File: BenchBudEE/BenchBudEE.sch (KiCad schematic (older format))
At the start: 0 parts

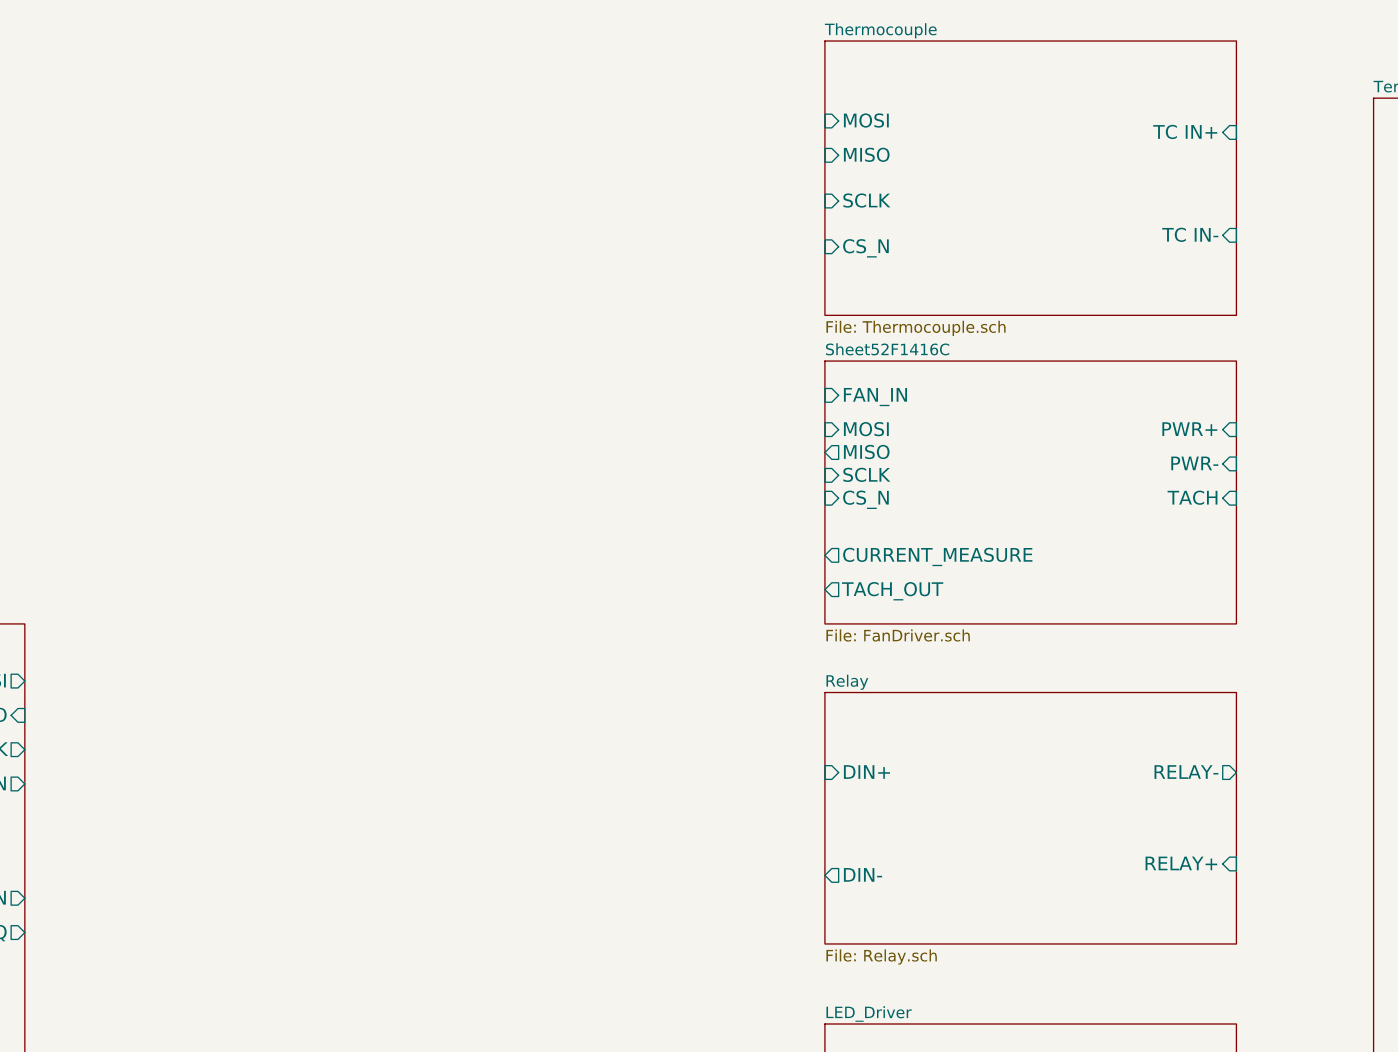
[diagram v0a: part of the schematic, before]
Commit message: Power module blocked out + added power adjustment monitor module
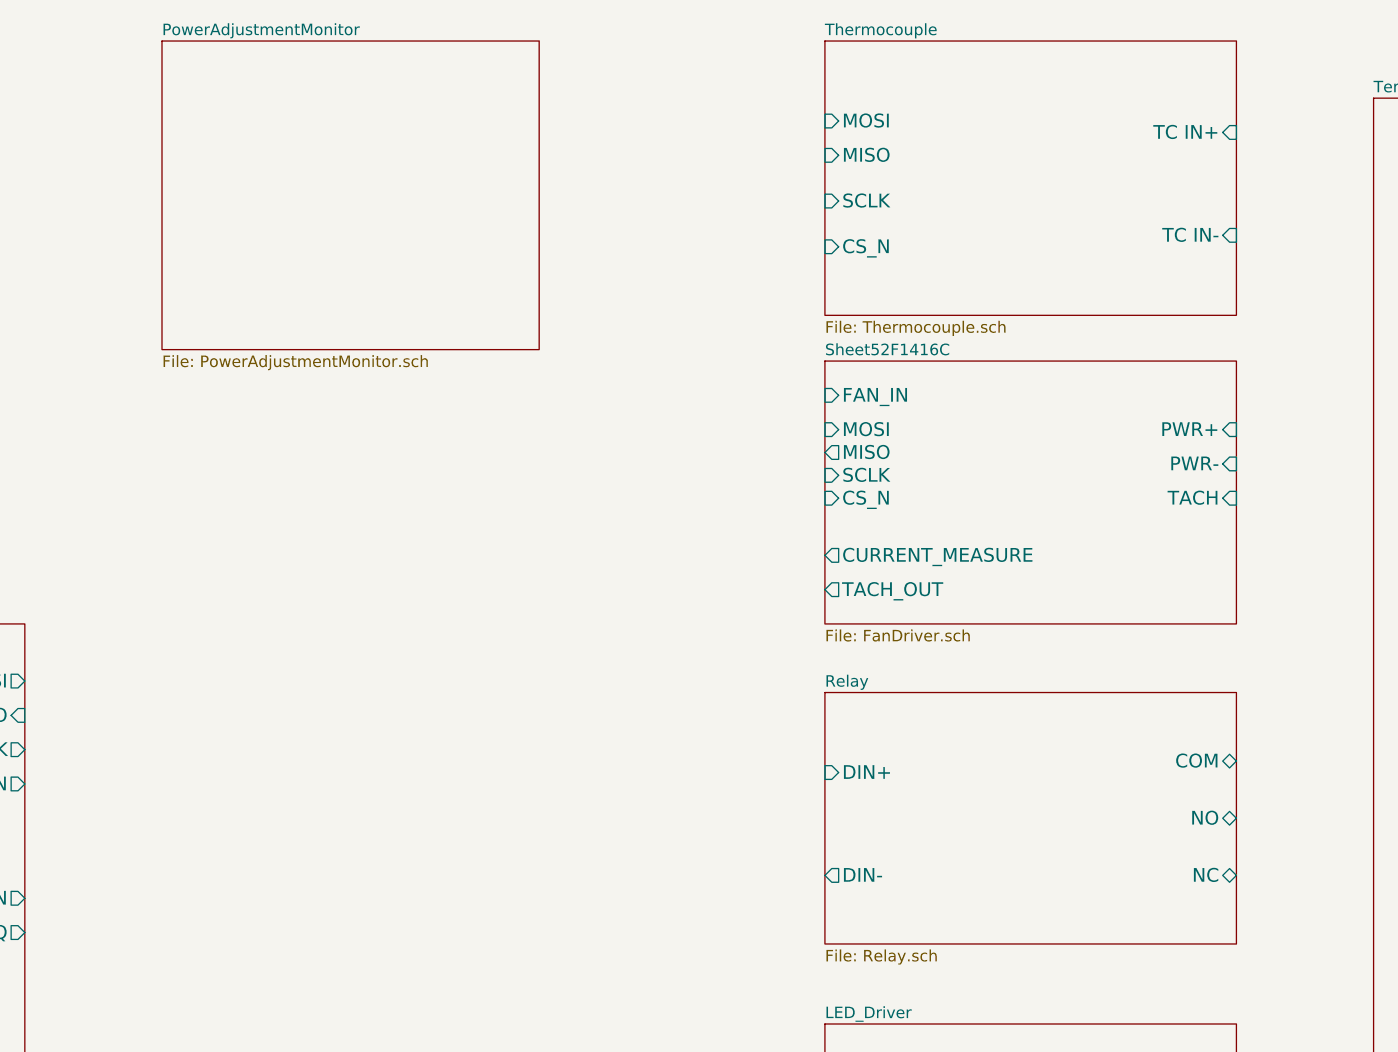
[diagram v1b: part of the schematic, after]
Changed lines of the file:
@@
 $Descr A4 11693 8268
 encoding utf-8
-Sheet 1 8
+Sheet 1 9
 Title ""
 Date "5 feb 2014"
@@
 F2 "DIN+" I L 7400 4250 60
 F3 "DIN-" O L 7400 4700 60
-F4 "RELAY-" O R 9200 4250 60
-F5 "RELAY+" I R 9200 4650 60
+F4 "NO" B R 9200 4450 60
+F5 "NC" B R 9200 4700 60
+F6 "COM" B R 9200 4200 60
 $EndSheet
 $Sheet
@@
 F7 "CS_N" I L 7400 1950 60
 $EndSheet
+$Sheet
+S 4500 1050 1650 1350
+U 52F2C572
+F0 "PowerAdjustmentMonitor" 50
+F1 "PowerAdjustmentMonitor.sch" 50
+$EndSheet
 $EndSCHEMATC

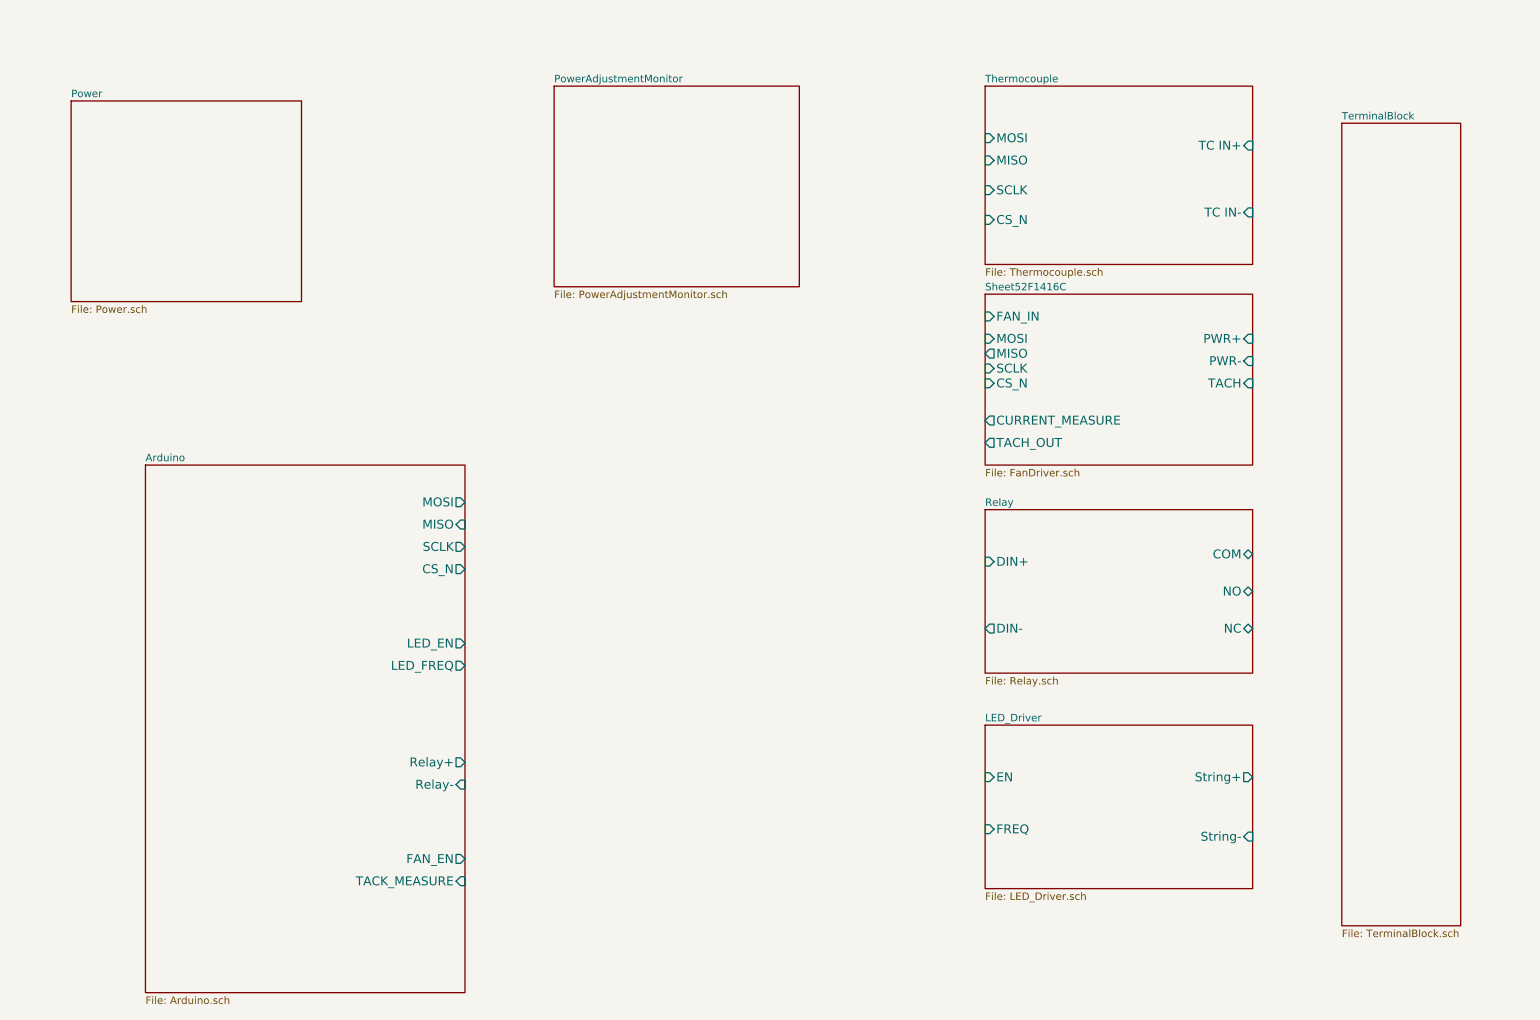
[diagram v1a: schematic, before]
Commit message: Power monitor module blocked out (needs tidying)
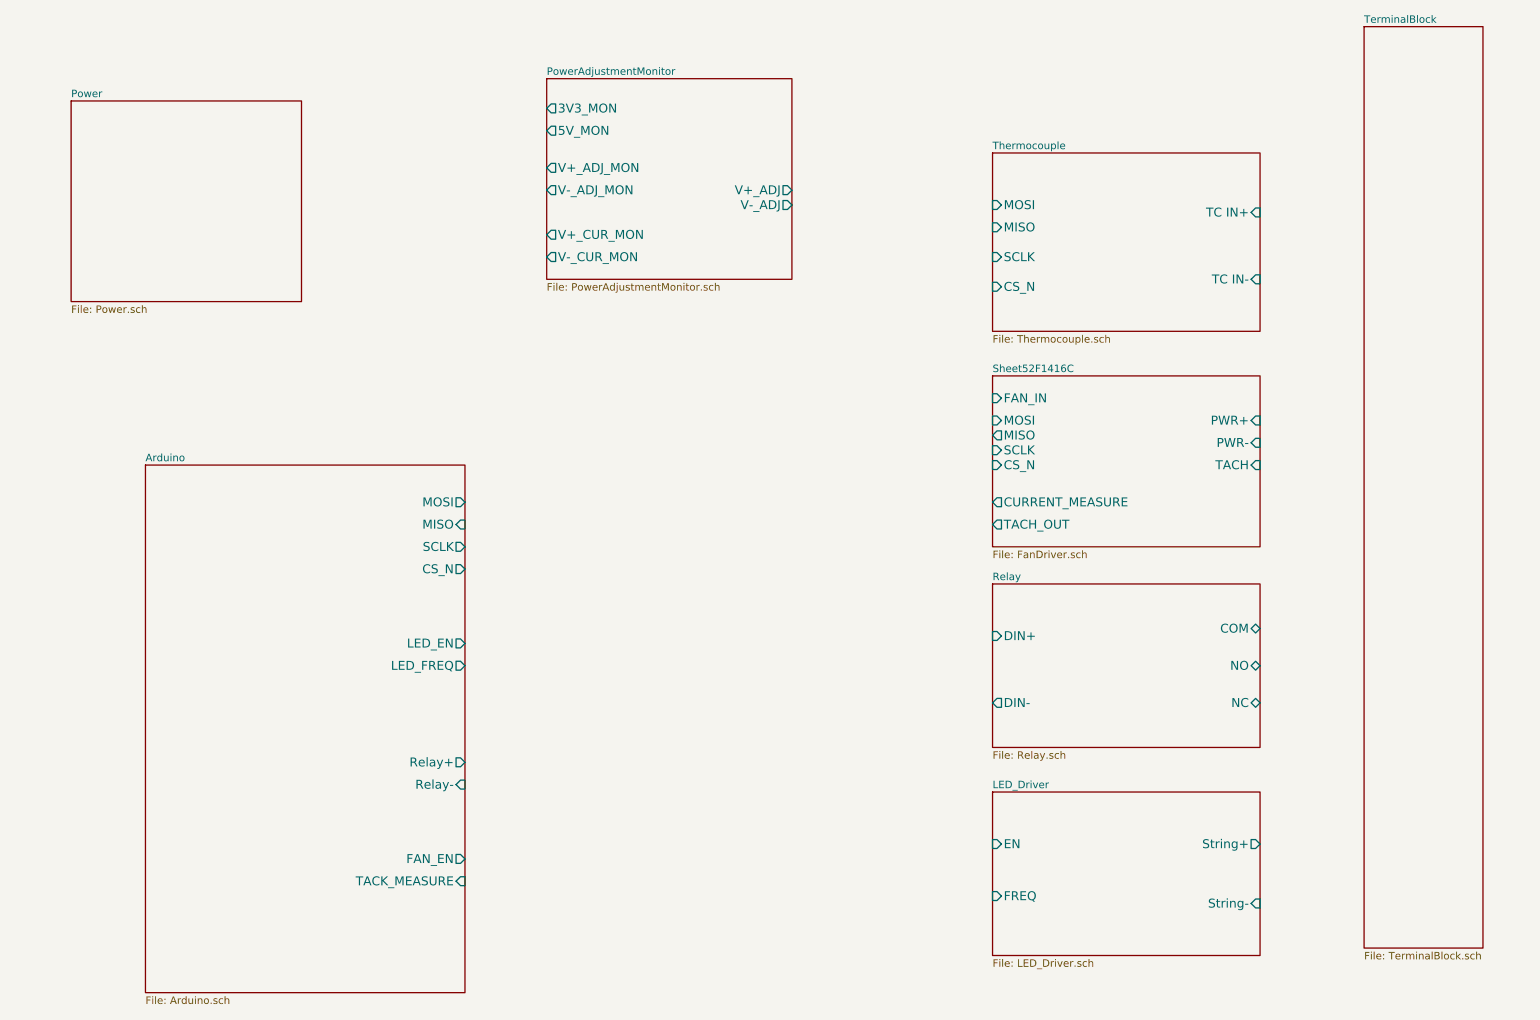
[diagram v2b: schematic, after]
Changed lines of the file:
@@
 Sheet 1 9
 Title ""
-Date "5 feb 2014"
+Date "6 feb 2014"
 Rev ""
 Comp ""
@@
 $EndSheet
 $Sheet
-S 7400 3900 1800 1100
+S 7450 4400 1800 1100
 U 52F1423A
 F0 "Relay" 50
 F1 "Relay.sch" 50
-F2 "DIN+" I L 7400 4250 60
-F3 "DIN-" O L 7400 4700 60
-F4 "NO" B R 9200 4450 60
-F5 "NC" B R 9200 4700 60
-F6 "COM" B R 9200 4200 60
+F2 "DIN+" I L 7450 4750 60
+F3 "DIN-" O L 7450 5200 60
+F4 "NO" B R 9250 4950 60
+F5 "NC" B R 9250 5200 60
+F6 "COM" B R 9250 4700 60
 $EndSheet
 $Sheet
-S 7400 5350 1800 1100
+S 7450 5800 1800 1100
 U 52F14293
 F0 "LED_Driver" 50
 F1 "LED_Driver.sch" 50
-F2 "EN" I L 7400 5700 60
-F3 "FREQ" I L 7400 6050 60
-F4 "String+" O R 9200 5700 60
-F5 "String-" I R 9200 6100 60
+F2 "EN" I L 7450 6150 60
+F3 "FREQ" I L 7450 6500 60
+F4 "String+" O R 9250 6150 60
+F5 "String-" I R 9250 6550 60
 $EndSheet
 $Sheet
-S 9800 1300 800  5400
+S 9950 650  800  6200
 U 52F142CF
 F0 "TerminalBlock" 50
@@
 $EndSheet
 $Sheet
-S 7400 2450 1800 1150
+S 7450 3000 1800 1150
 U 52F1416D
 F0 "Sheet52F1416C" 50
 F1 "FanDriver.sch" 50
-F2 "PWR+" I R 9200 2750 60
-F3 "PWR-" I R 9200 2900 60
-F4 "FAN_IN" I L 7400 2600 60
-F5 "TACH" I R 9200 3050 60
-F6 "TACH_OUT" O L 7400 3450 60
-F7 "CURRENT_MEASURE" O L 7400 3300 60
-F8 "MOSI" I L 7400 2750 60
-F9 "MISO" O L 7400 2850 60
-F10 "SCLK" I L 7400 2950 60
-F11 "CS_N" I L 7400 3050 60
+F2 "PWR+" I R 9250 3300 60
+F3 "PWR-" I R 9250 3450 60
+F4 "FAN_IN" I L 7450 3150 60
+F5 "TACH" I R 9250 3600 60
+F6 "TACH_OUT" O L 7450 4000 60
+F7 "CURRENT_MEASURE" O L 7450 3850 60
+F8 "MOSI" I L 7450 3300 60
+F9 "MISO" O L 7450 3400 60
+F10 "SCLK" I L 7450 3500 60
+F11 "CS_N" I L 7450 3600 60
 $EndSheet
 $Sheet
-S 7400 1050 1800 1200
+S 7450 1500 1800 1200
 U 52F14139
 F0 "Thermocouple" 50
 F1 "Thermocouple.sch" 50
-F2 "TC IN+" I R 9200 1450 60
-F3 "TC IN-" I R 9200 1900 60
-F4 "MISO" I L 7400 1550 60
-F5 "MOSI" I L 7400 1400 60
-F6 "SCLK" I L 7400 1750 60
-F7 "CS_N" I L 7400 1950 60
+F2 "TC IN+" I R 9250 1900 60
+F3 "TC IN-" I R 9250 2350 60
+F4 "MISO" I L 7450 2000 60
+F5 "MOSI" I L 7450 1850 60
+F6 "SCLK" I L 7450 2200 60
+F7 "CS_N" I L 7450 2400 60
 $EndSheet
 $Sheet
-S 4500 1050 1650 1350
+S 4450 1000 1650 1350
 U 52F2C572
 F0 "PowerAdjustmentMonitor" 50
 F1 "PowerAdjustmentMonitor.sch" 50
+F2 "V+_ADJ" O R 6100 1750 60
+F3 "V-_ADJ" O R 6100 1850 60
+F4 "3V3_MON" O L 4450 1200 60
+F5 "5V_MON" O L 4450 1350 60
+F6 "V+_ADJ_MON" O L 4450 1600 60
+F7 "V-_ADJ_MON" O L 4450 1750 60
+F8 "V+_CUR_MON" O L 4450 2050 60
+F9 "V-_CUR_MON" O L 4450 2200 60
 $EndSheet
 $EndSCHEMATC

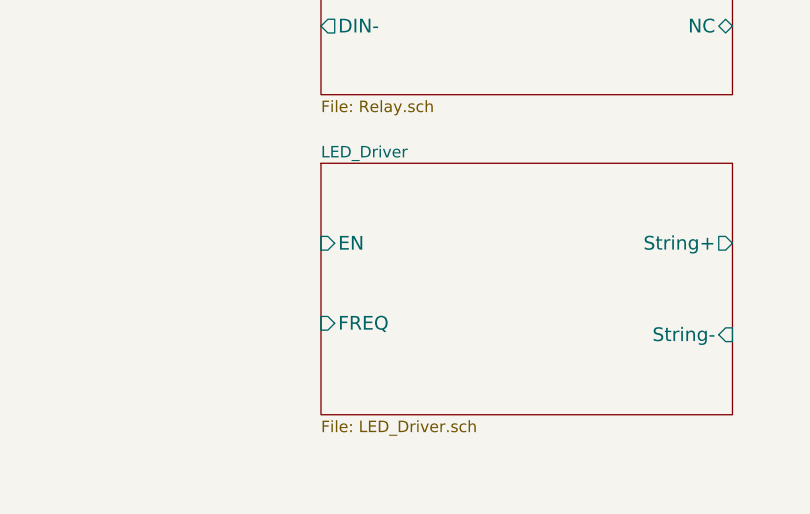
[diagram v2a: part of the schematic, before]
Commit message: LED Driver module sketched out from AP5726 chip
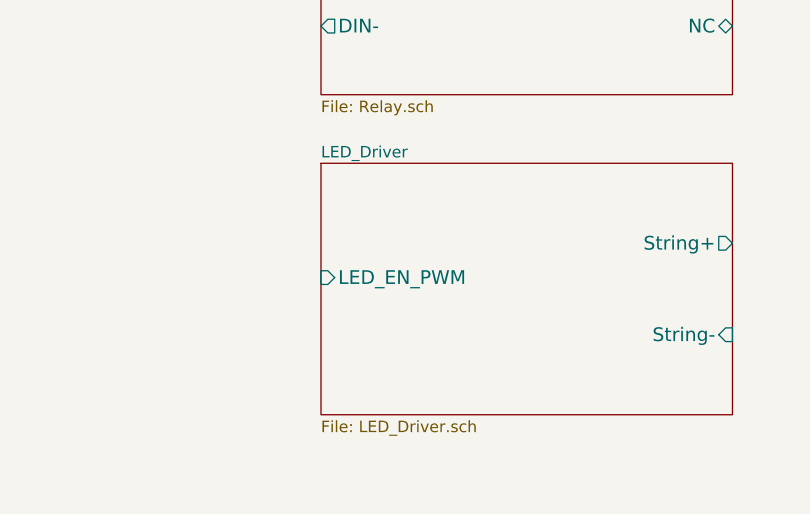
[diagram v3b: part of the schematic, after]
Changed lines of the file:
@@
 F0 "LED_Driver" 50
 F1 "LED_Driver.sch" 50
-F2 "EN" I L 7450 6150 60
-F3 "FREQ" I L 7450 6500 60
-F4 "String+" O R 9250 6150 60
-F5 "String-" I R 9250 6550 60
+F2 "String+" O R 9250 6150 60
+F3 "String-" I R 9250 6550 60
+F4 "LED_EN_PWM" I L 7450 6300 60
 $EndSheet
 $Sheet
